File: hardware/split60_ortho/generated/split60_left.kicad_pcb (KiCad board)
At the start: 2 copper layers, 186.9 x 159.8 mm, 65 parts

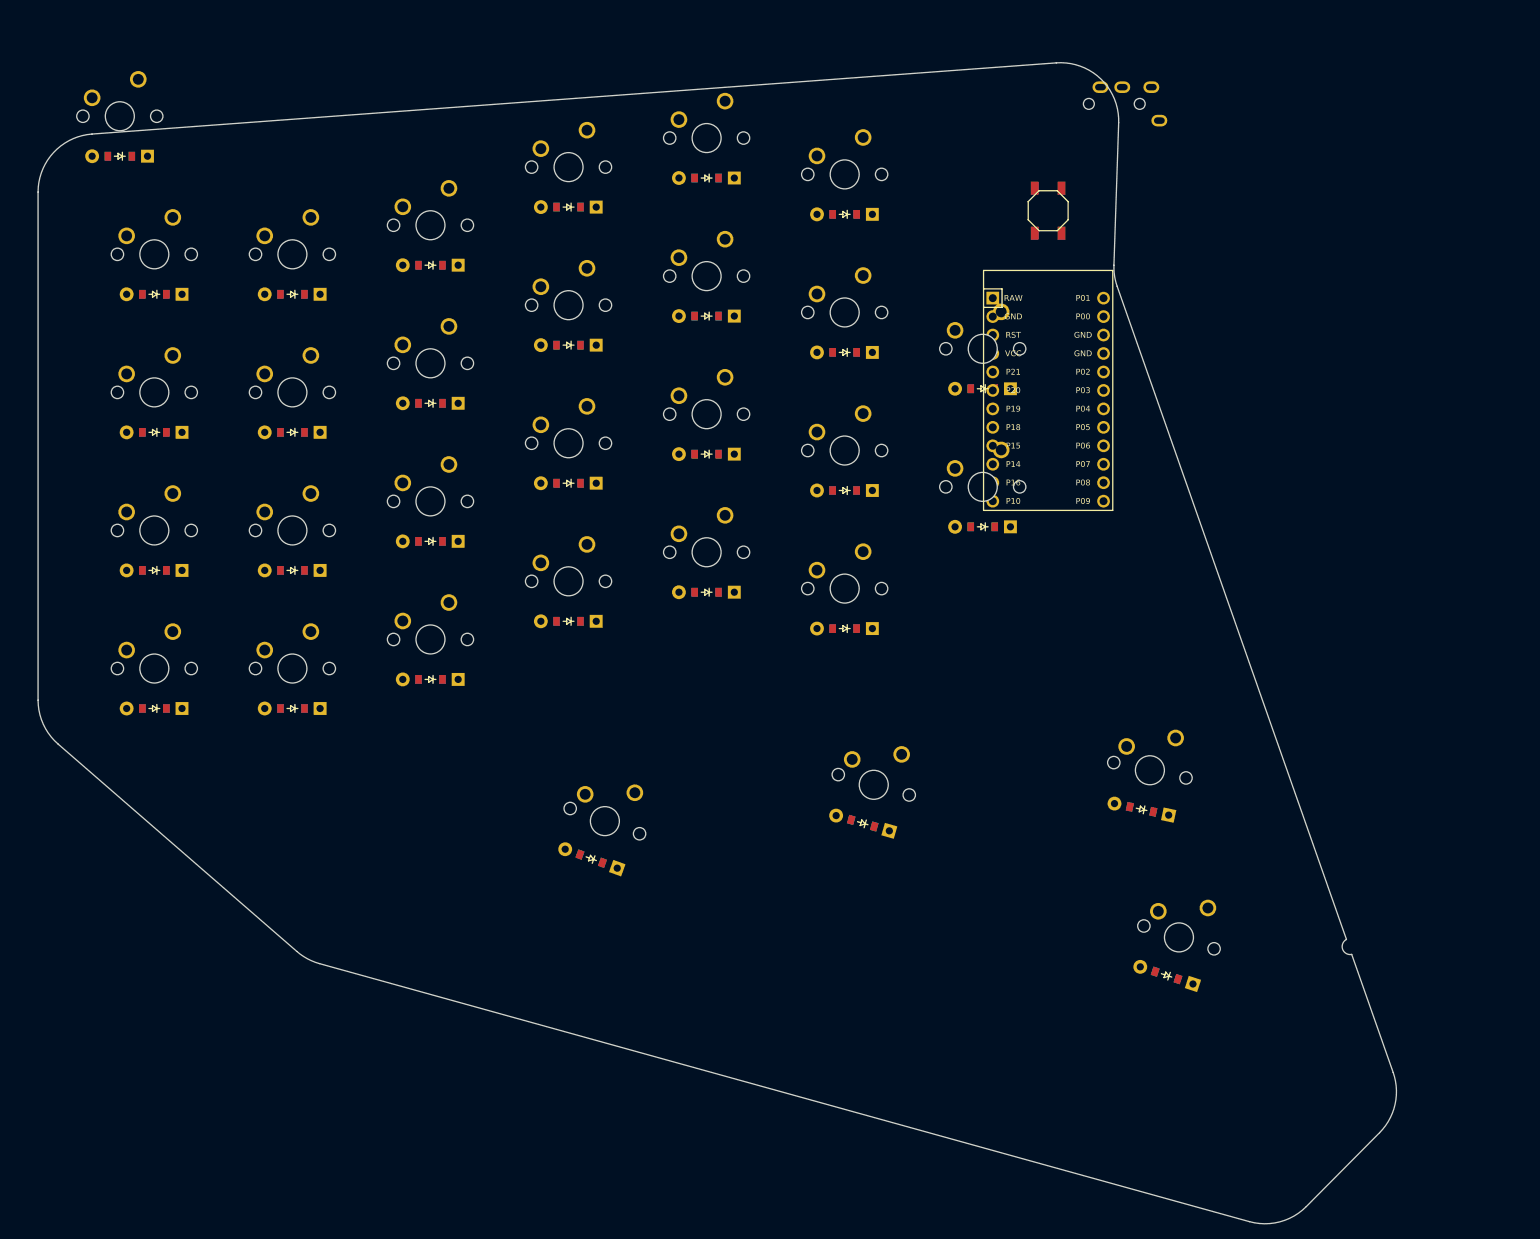
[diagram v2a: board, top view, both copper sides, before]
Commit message: Rework QWERT stagger and thumb cluster
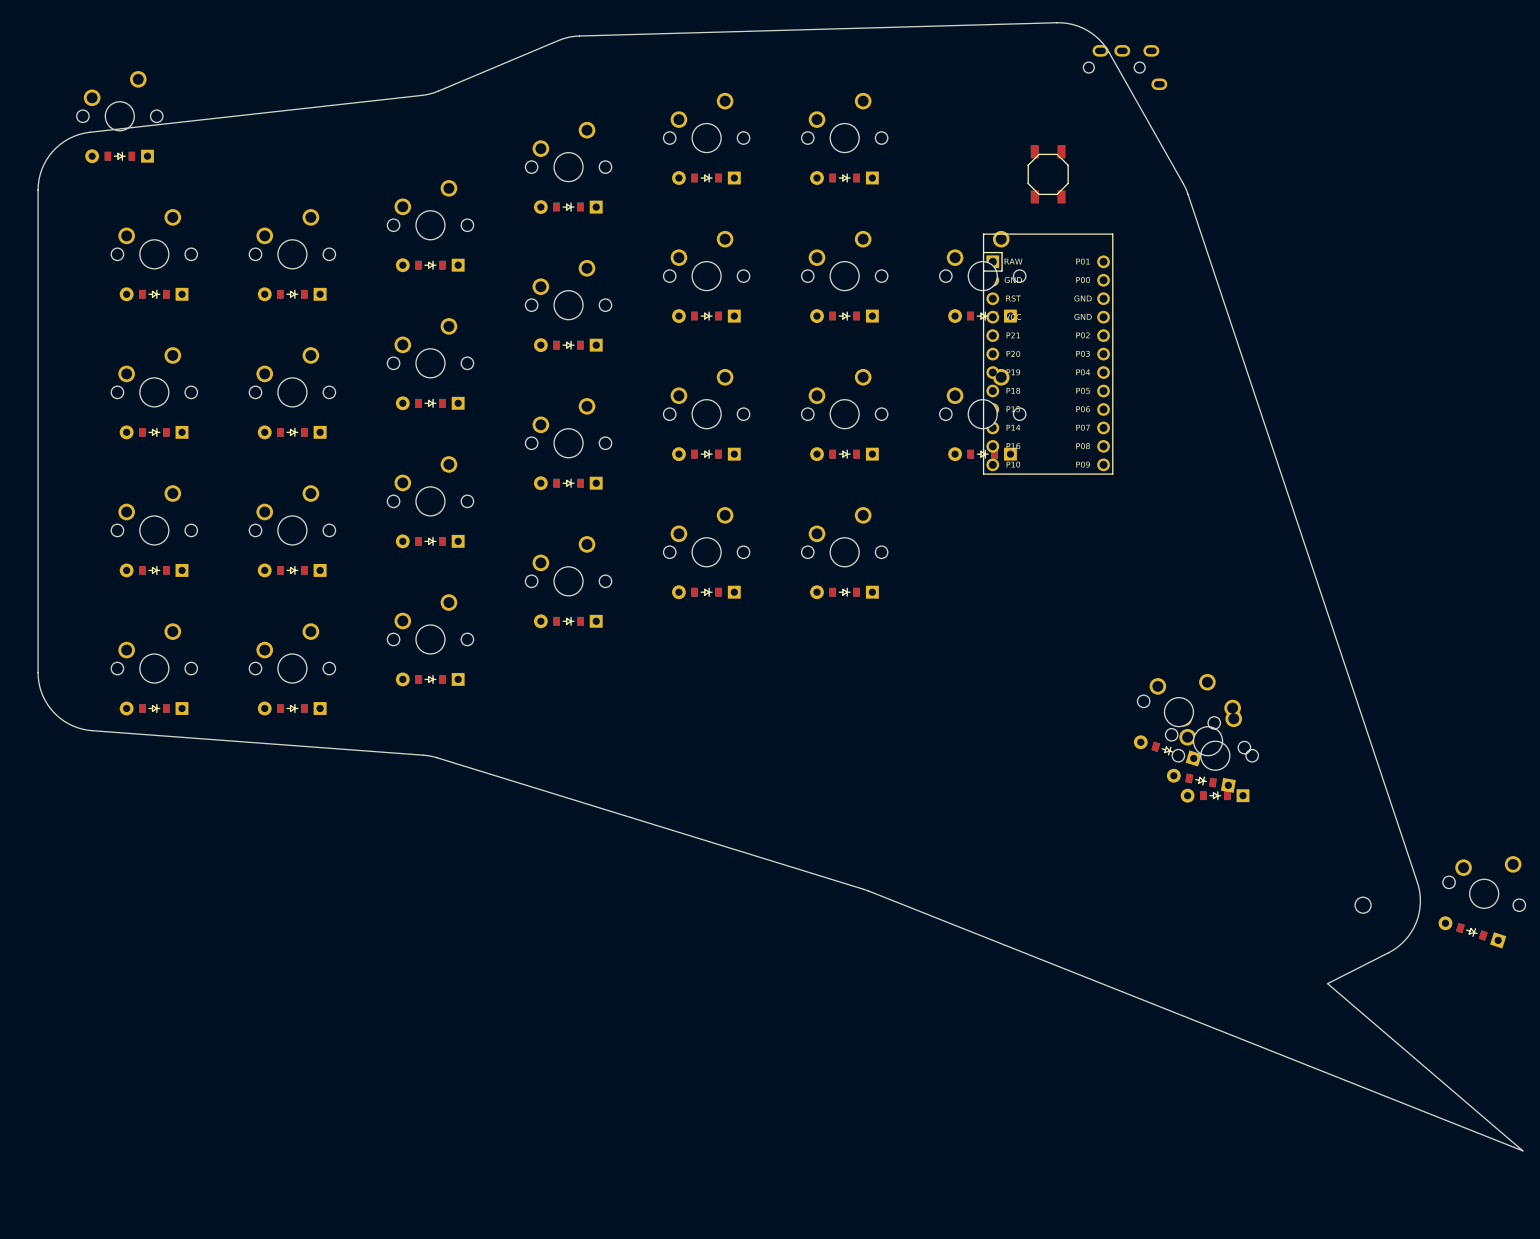
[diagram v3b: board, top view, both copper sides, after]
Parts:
- moved D28 86.3 mm to (146.0, 17.5), turned to 180 degrees
- moved S28 84.5 mm to (146.0, 12.0), turned to 0 degrees
- moved D29 46.9 mm to (144.0, 15.4), turned to 170 degrees
- moved S29 46.4 mm to (145.0, 10.0), turned to -10 degrees
- moved D31 42.4 mm to (181.3, 36.2)
- moved S31 42.4 mm to (183.0, 31.0)
- moved D26 10.0 mm to (114.0, -29.5)
- moved D27 10.0 mm to (114.0, -48.5)
- moved S26 10.0 mm to (114.0, -35.0)
- moved S27 10.0 mm to (114.0, -54.0)
- moved S30 8.94 mm to (141.0, 6.00), turned to -17 degrees
- moved D30 8.86 mm to (139.4, 11.3), turned to 163 degrees
- moved B1 5.00 mm to (123.0, -68.0)
- moved D22 5.00 mm to (95.0, -10.5)
- moved D23 5.00 mm to (95.0, -29.5)
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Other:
- board size 186.9 x 159.8 mm -> 204.3 x 155.2 mm

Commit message: Adjust thumb cluster preview layout
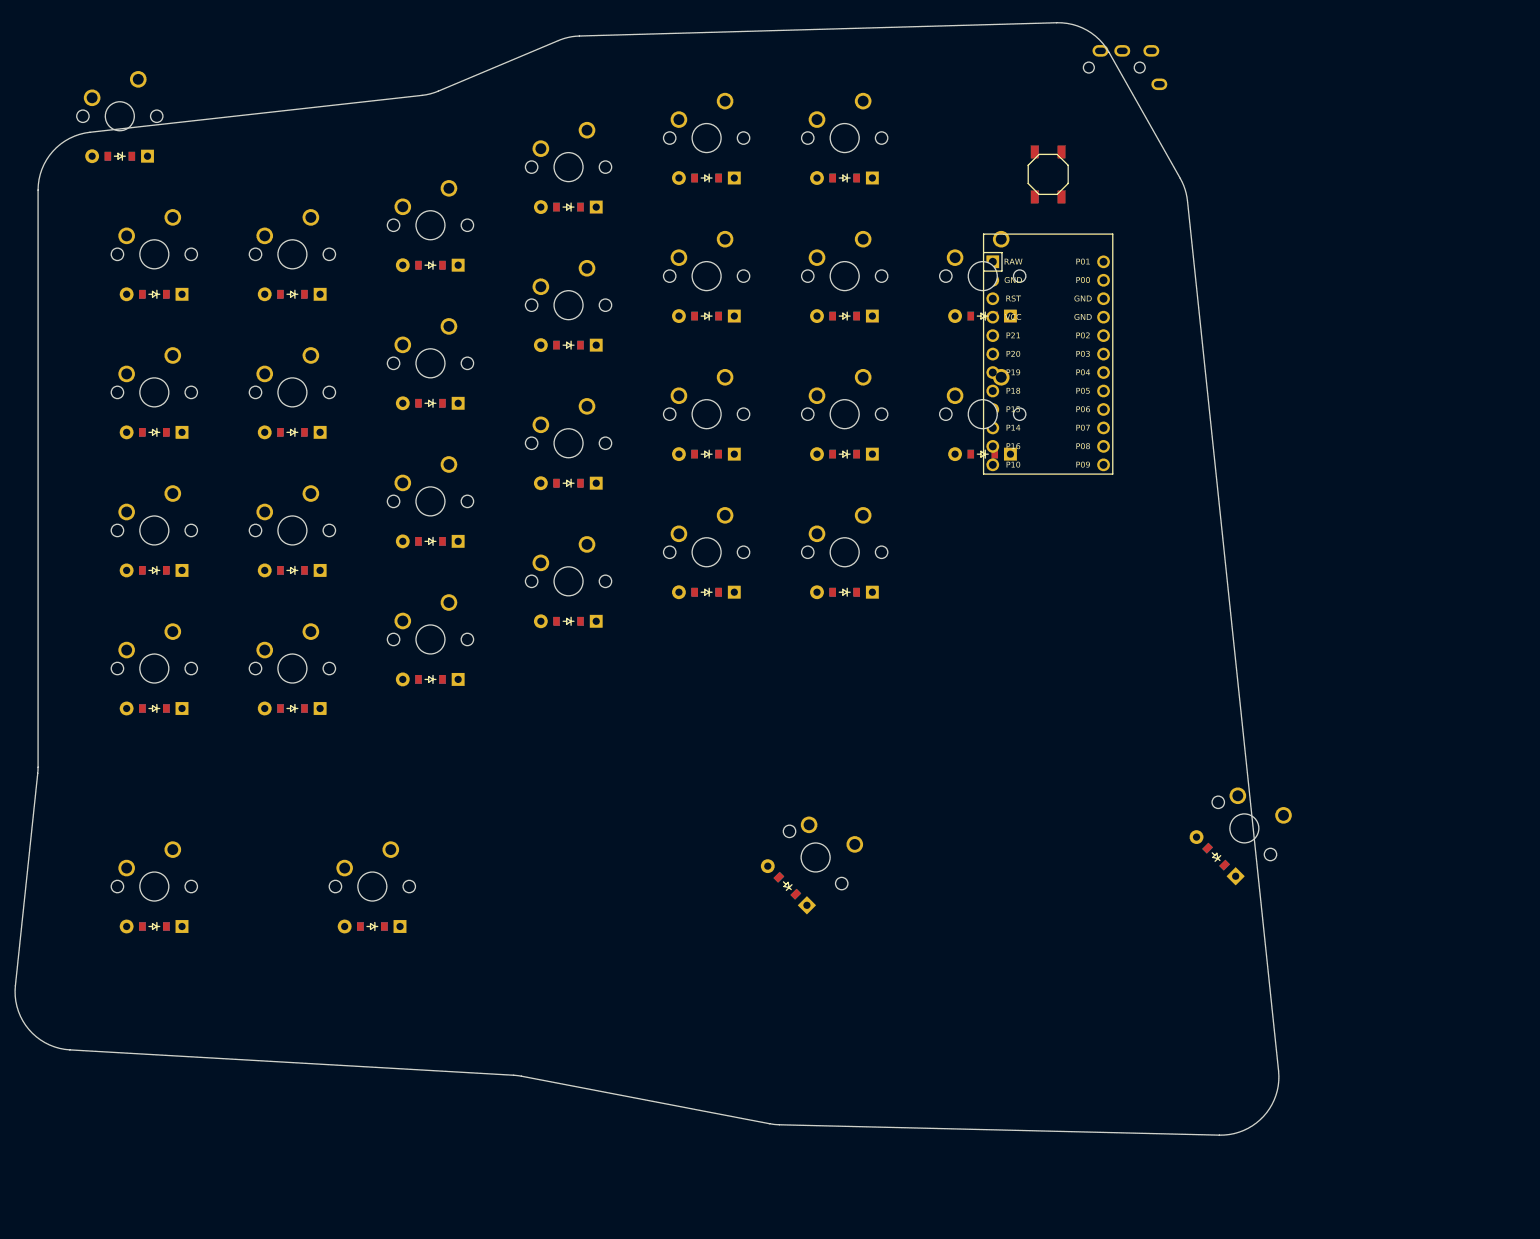
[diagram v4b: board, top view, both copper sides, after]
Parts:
- moved S31 183.0 mm to (0.00, 30.0), turned to 0 degrees
- moved D31 181.3 mm to (0.00, 35.5), turned to 180 degrees
- moved D28 117.4 mm to (30.0, 35.5)
- moved S28 117.4 mm to (30.0, 30.0)
- moved D29 58.7 mm to (87.1, 29.9), turned to 135 degrees
- moved S29 56.3 mm to (91.0, 26.0), turned to -45 degrees
- moved S30 18.4 mm to (150.0, 22.0), turned to -45 degrees
- moved D30 16.1 mm to (146.1, 25.9), turned to 135 degrees
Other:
- board size 204.3 x 155.2 mm -> 173.9 x 153.1 mm
